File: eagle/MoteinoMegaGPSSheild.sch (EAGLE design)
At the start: 10 parts, among them Q2 NDP6020P P-CHANNEL

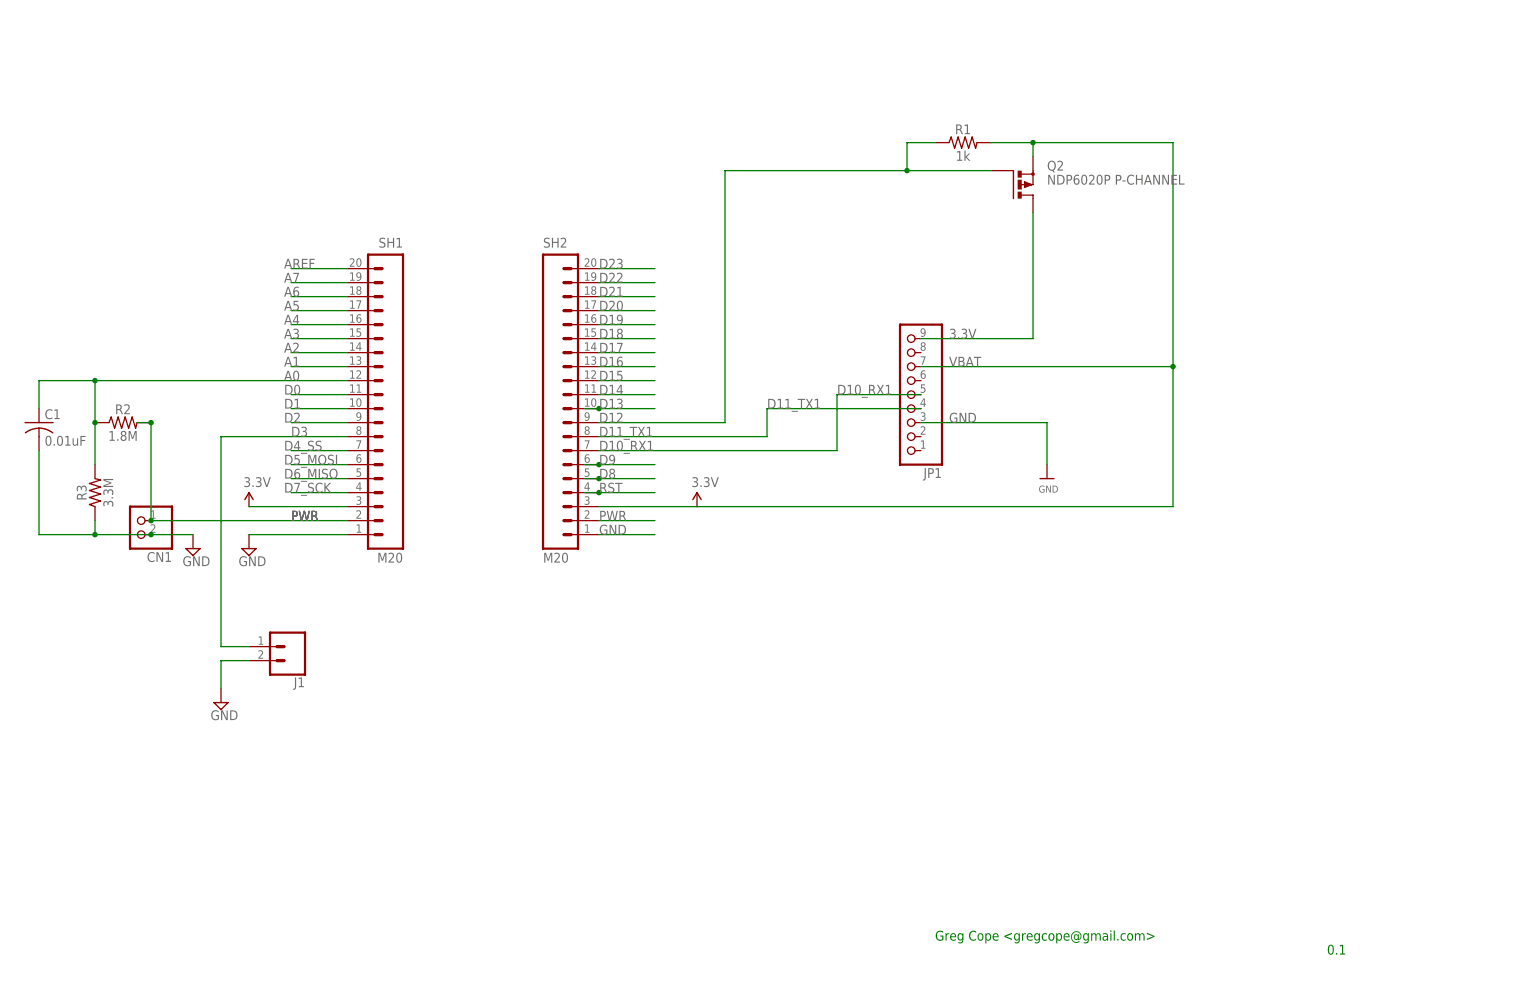
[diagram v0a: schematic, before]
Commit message: V0.2 No errors, Bottom layer copper pour
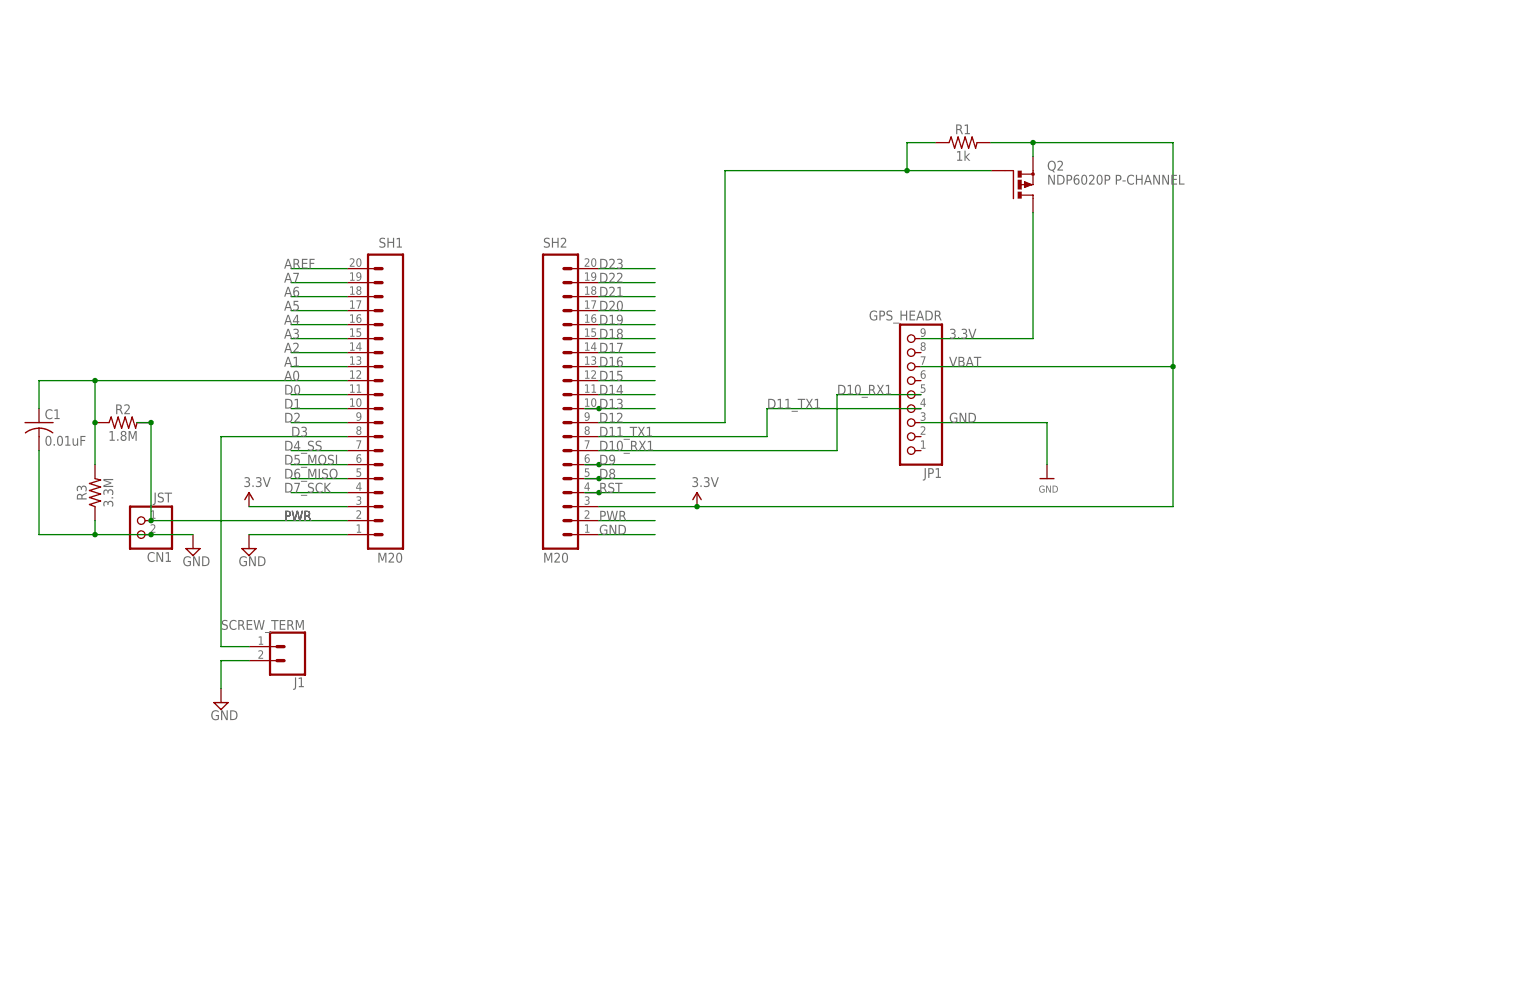
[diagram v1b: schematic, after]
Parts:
- CN1: value (none) -> JST
- J1: value (none) -> SCREW_TERM
- JP1: value (none) -> GPS_HEADR
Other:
- note removed: "0.1"
- note removed: "Greg Cope <gregcope@gmail.com>"
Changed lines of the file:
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@@
 <schematic xreflabel="%F%N/%S.%C%R" xrefpart="/%S.%C%R">
 <attributes>
+<attribute name="CNAME" value="MoteinoMega Ultimate GPS Sheild"/>
+<attribute name="CREVISION" value="0.2"/>
+<attribute name="DESIGNER" value="greg.cope@gmail.com"/>
 </attributes>
 <variantdefs>
@@
 <parts>
 <part name="U$12" library="microbuilder" deviceset="GND" device=""/>
-<part name="JP1" library="microbuilder" deviceset="HEADER-1X9" device="70MIL"/>
+<part name="JP1" library="microbuilder" deviceset="HEADER-1X9" device="70MIL" value="GPS_HEADR"/>
 <part name="P+2" library="SparkFun" deviceset="VCC" device="" value="3.3V"/>
 <part name="SUPPLY1" library="supply2" deviceset="GND" device=""/>
@@
 <part name="P+3" library="SparkFun" deviceset="VCC" device="" value="3.3V"/>
 <part name="R1" library="SparkFun-Resistors" deviceset="1KOHM" device="-HORIZ-1/4W-1%" value="1k"/>
-<part name="CN1" library="adafruit" deviceset="JST_2PIN" device="-THM"/>
+<part name="CN1" library="adafruit" deviceset="JST_2PIN" device="-THM" value="JST"/>
 <part name="SUPPLY2" library="supply2" deviceset="GND" device=""/>
 <part name="R2" library="SparkFun-Resistors" deviceset="1MOHM" device="-HORIZ_KIT-1/6W-5%" value="1.8M"/>
@@
 <part name="C1" library="adafruit" deviceset="C-US" device="075-032X103" value="0.01uF"/>
 <part name="Q2" library="transistor-power" deviceset="PMOSFET_P" device="TO220BV" value="NDP6020P P-CHANNEL"/>
-<part name="J1" library="SparkFun-Retired" deviceset="CONN_02" device="POLAR"/>
+<part name="J1" library="SparkFun-Retired" deviceset="CONN_02" device="POLAR" value="SCREW_TERM"/>
 <part name="SUPPLY3" library="supply2" deviceset="GND" device=""/>
+<part name="FRAME1" library="SparkFun-Aesthetics" deviceset="FRAME-A4L" device=""/>
 </parts>
 <sheets>
 <sheet>
 <plain>
-<text x="167.64" y="10.16" size="1.778" layer="91">Greg Cope &lt;gregcope@gmail.com&gt;</text>
-<text x="238.76" y="7.62" size="1.778" layer="91">0.1</text>
 </plain>
 <instances>
@@
 <instance part="J1" gate="G$1" x="50.8" y="63.5" rot="R180"/>
 <instance part="SUPPLY3" gate="GND" x="38.1" y="53.34"/>
+<instance part="FRAME1" gate="G$1" x="0" y="0"/>
 </instances>
 <busses>
@@
 <junction x="25.4" y="104.14"/>
 <pinref part="SH1" gate="G$1" pin="2"/>
-<wire x1="60.96" y1="86.36" x2="53.34" y2="86.36" width="0.1524" layer="91"/>
-<label x="50.8" y="86.36" size="1.778" layer="95"/>
-<label x="50.8" y="86.36" size="1.778" layer="95"/>
-<label x="50.8" y="86.36" size="1.778" layer="95"/>
-<wire x1="53.34" y1="86.36" x2="50.8" y2="86.36" width="0.1524" layer="91"/>
-<wire x1="25.4" y1="86.36" x2="50.8" y2="86.36" width="0.1524" layer="91"/>
+<label x="49.53" y="86.36" size="1.778" layer="95"/>
+<label x="49.53" y="86.36" size="1.778" layer="95"/>
+<label x="49.53" y="86.36" size="1.778" layer="95"/>
+<wire x1="25.4" y1="86.36" x2="60.96" y2="86.36" width="0.1524" layer="91"/>
 <junction x="25.4" y="86.36"/>
 </segment>
@@
 <junction x="185.42" y="154.94"/>
 <pinref part="Q2" gate="G$1" pin="S"/>
+<junction x="124.46" y="88.9"/>
 </segment>
 </net>
@@
 </sheet>
 </sheets>
+<errors>
+</errors>
 </schematic>
 </drawing>

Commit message: v0.3 ... GSM plus right Mega headers
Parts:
- removed SH1, SH2: M20, SparkFun-Connectors:M20
- added FONA_GSM: HEADER, adafruit2:PINHD-1X12-CB
- added J2, J3, J4, J5, J6: SCREW_TERM, SparkFun-Connectors:CONN_023.5MM-NO_SILK
- added U$1: MOTEINO_MEGA_SIMPLE, Moteino:MOTEINO_MEGA_SIMPLE
- C1: value 0.01uF -> 0.1uF
- J1: device SparkFun-Retired:CONN_02POLAR -> SparkFun-Connectors:CONN_023.5MM-NO_SILK
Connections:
- removed net A5: SH1.17
- removed net A6: SH1.18
- removed net A7: SH1.19
- removed net AREF: SH1.20
- removed net D0: SH1.11
- removed net D13: SH2.10
- removed net D14: SH2.11
- removed net D15: SH2.12
- removed net D16: SH2.13
- removed net D17: SH2.14
- removed net D18: SH2.15
- removed net D19: SH2.16
- removed net D2: SH1.9
- removed net D20: SH2.17
- removed net D21: SH2.18
- removed net D22: SH2.19
- removed net D23: SH2.20
- removed net D4_SS: SH1.7
- removed net D5_MOSI: SH1.6
- removed net D6_MISO: SH1.5
- removed net D7_SCK: SH1.4
- removed net PWR: CN1.2, R2.2, SH1.2, SH2.2
- removed net RST: SH2.4
- removed net VBAT: JP1.7, Q2.S, R1.2, SH1.3, SH2.3
- new net D13_NETSTAT: FONA_GSM.2, U$1.D13
- new net D14_KEY: FONA_GSM.6, U$1.D14
- new net D18_PS: FONA_GSM.7, U$1.D18
- new net N$3: J6.2
- new net SPEAKER2+: FONA_GSM.10
- new net VIN: CN1.2, FONA_GSM.12, R2.2, U$1.VIN
- net 3.3V: now also FONA_GSM.1, JP1.7, Q2.S, R1.2, U$1.3V3_2
- net A0: now also U$1.A0; no longer SH1.12
- net A1: now also U$1.A1; no longer SH1.13
- net A2: now also J2.2, J3.2, U$1.A2; no longer SH1.14
- net A3: now also J5.2, U$1.A3; no longer SH1.15
- net A4: now also J6.1, U$1.A4; no longer SH1.16
- net D1: now also J4.2, U$1.D1; no longer SH1.10
- net D10_RX1: now also U$1.D10_RX1; no longer SH2.7
- net D11_TX1: now also U$1.D11_TX1; no longer SH2.8
- net D12: now also U$1.D12; no longer SH2.9
- net D3: now also J1.2, U$1.D3; no longer J1.1, SH1.8
- net D8: now also FONA_GSM.4, U$1.D8_RX0; no longer SH2.5
- net D9: now also FONA_GSM.3, U$1.D9_TX0; no longer SH2.6
- net GND: now also FONA_GSM.11, J1.1, J2.1, J3.1, J4.1, J5.1, U$1.GND1, U$1.GND2; no longer J1.2, SH1.1, SH2.1
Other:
- moved on the sheet: J1

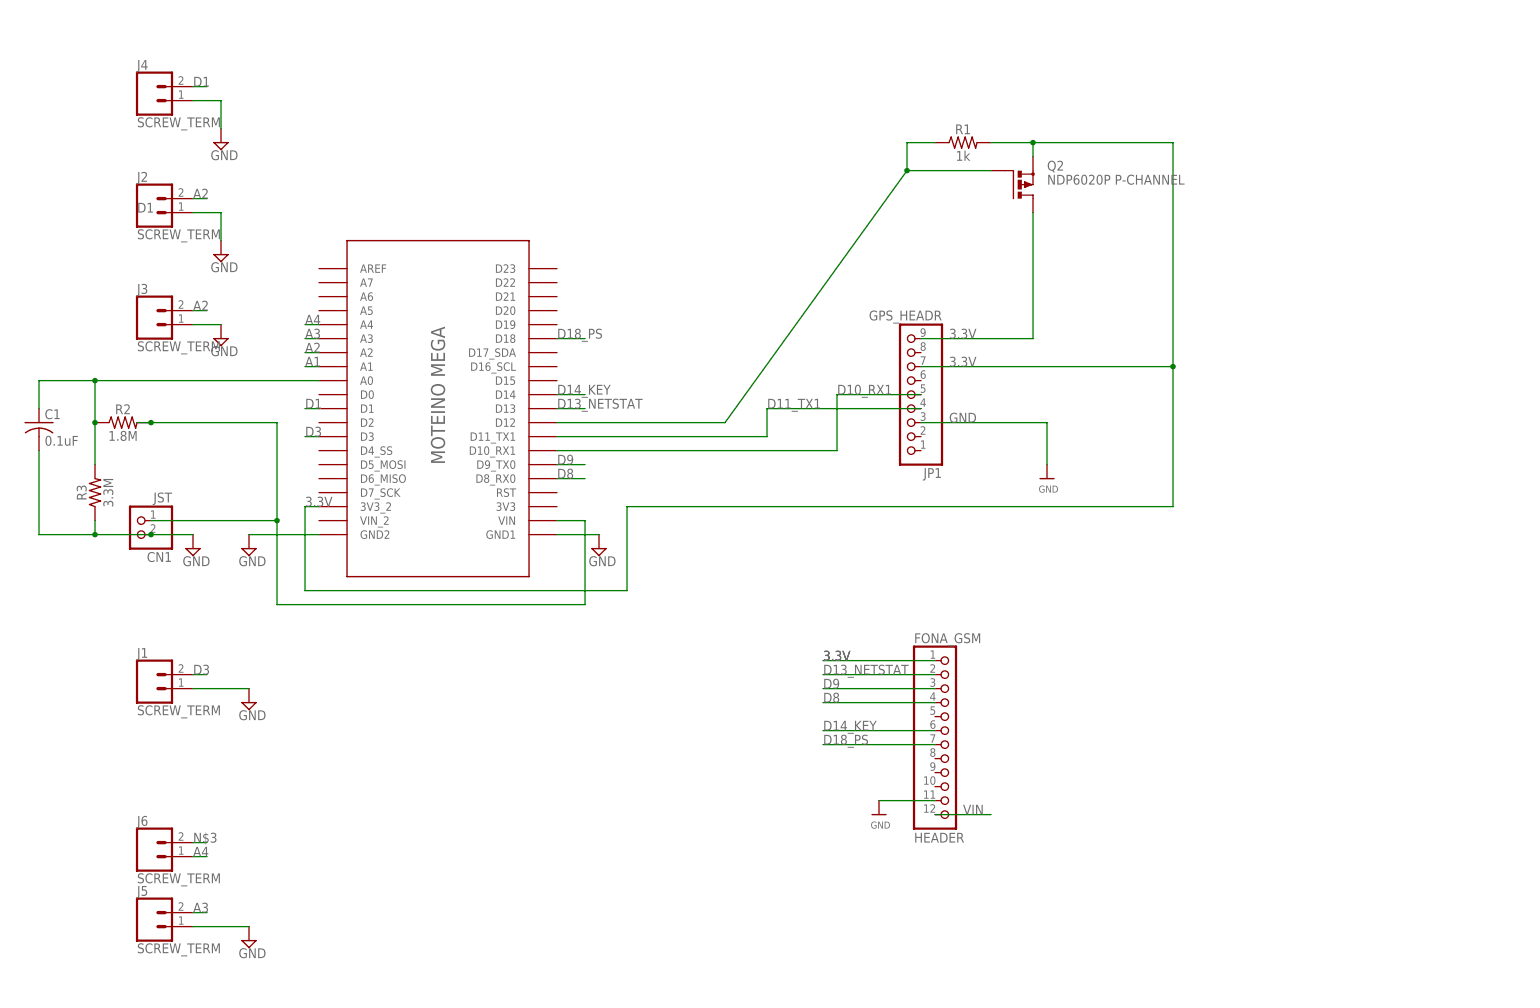
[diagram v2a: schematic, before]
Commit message: Removing PDFs
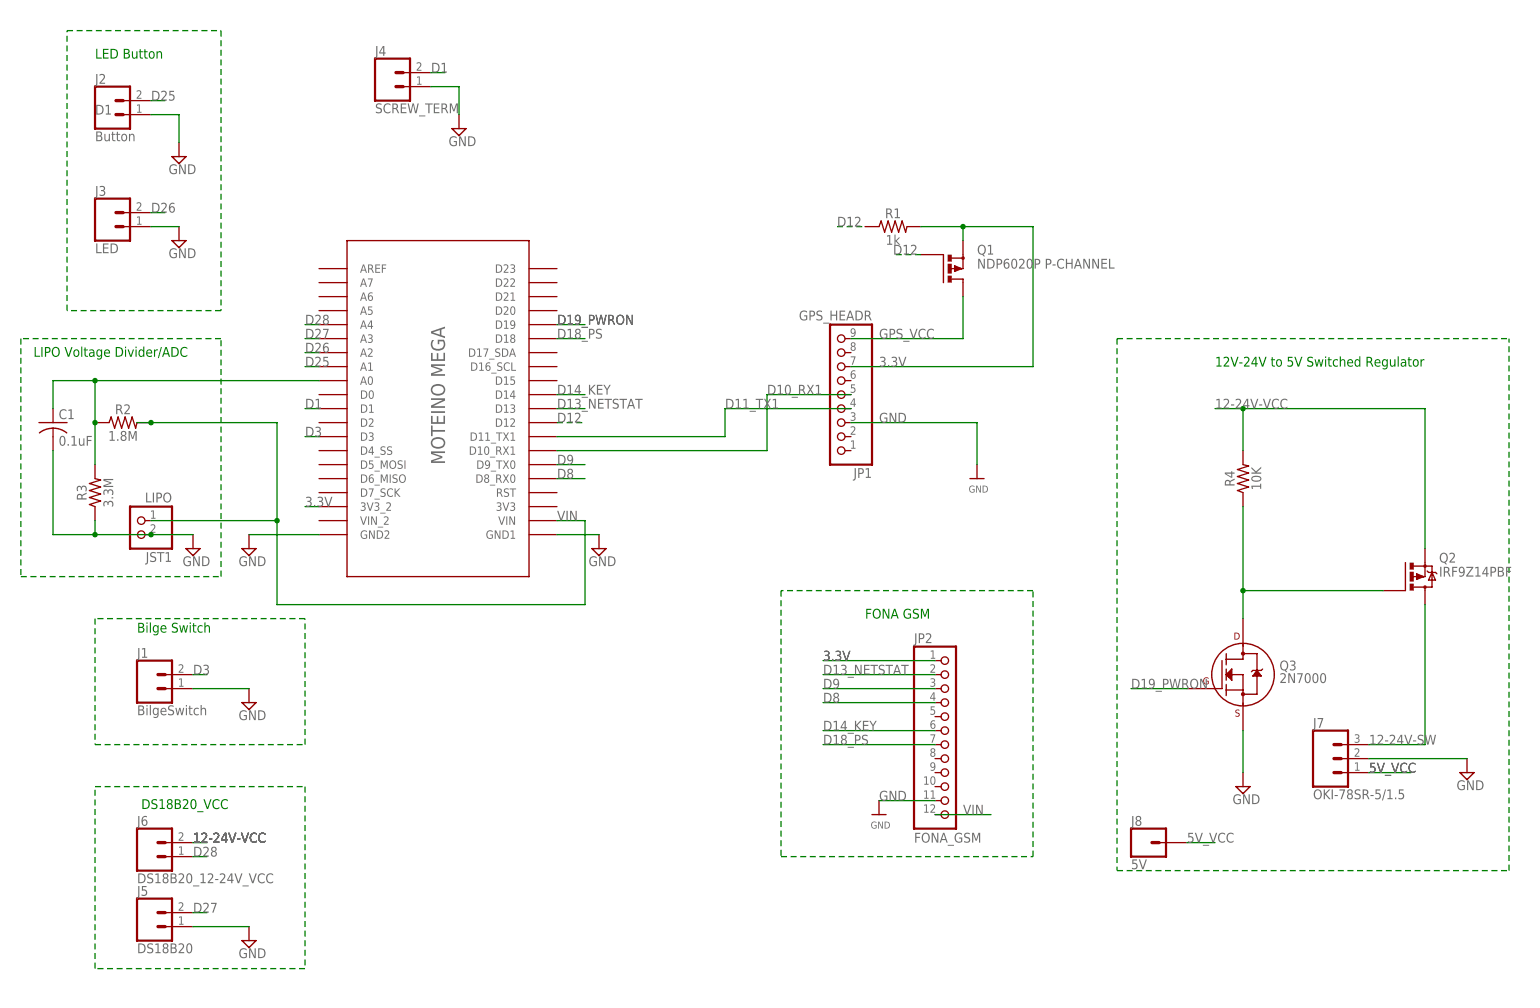
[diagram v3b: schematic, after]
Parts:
- added J7: OKI-78SR-5/1.5, SparkFun-Connectors:CONN_03
- added J8: 5V, SparkFun-Connectors:CONN_01
- added Q1: NDP6020P P-CHANNEL, transistor-power:PMOSFET_PTO220BV
- added Q3: 2N7000, transistors:2N7002_TO92
- added R4: 10K, SparkFun-Resistors:1MOHM-HORIZ_KIT-1/6W-5%
- J1: value SCREW_TERM -> BilgeSwitch
- J2: value SCREW_TERM -> Button
- J3: value SCREW_TERM -> LED
- J5: value SCREW_TERM -> DS18B20
- J6: value SCREW_TERM -> DS18B20_12-24V_VCC
- JP2: value HEADER -> FONA_GSM
- JST1: value JST -> LIPO
- MOTEINO_MEGA: value MOTEINO_MEGA_SIMPLE -> HEADERS
- Q2: value NDP6020P P-CHANNEL -> IRF9Z14PBF; device transistor-power:PMOSFET_PTO220BV -> transistor-power:IRF9530
- renumbered CN1 to JST1, FONA_GSM to JP2, U$1 to MOTEINO_MEGA
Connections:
- net A3 renamed D27
- net A4 renamed D28
- removed net A1: MOTEINO_MEGA.A1
- removed net A2: J2.2, J3.2, MOTEINO_MEGA.A2
- removed net N$3: J6.2
- new net 12-24V-SW: J7.3, Q2.D
- new net 12-24V-VCC: J6.2, Q2.S, R4.2
- new net 5V_VCC: J7.1, J8.1
- new net D19_PWRON: MOTEINO_MEGA.D19, Q3.G
- new net D25: J2.2, MOTEINO_MEGA.A1
- new net D26: J3.2, MOTEINO_MEGA.A2
- new net GPS_VCC: JP1.9, Q1.D
- new net N$2: Q2.G, Q3.D, R4.1
- net 3.3V: now also Q1.S; no longer JP1.9, Q2.D, Q2.S
- net D12: now also Q1.G; no longer Q2.G
- net GND: now also J7.2, Q3.S
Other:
- note added: "12V-24V to 5V Switched Regulator"
- note added: "Bilge Switch"
- note added: "DS18B20_VCC"
- note added: "FONA GSM"
- note added: "LED Button"
- note added: "LIPO Voltage Divider/ADC"
- moved on the sheet: C1, J2, J3, J4, JP1, R1
